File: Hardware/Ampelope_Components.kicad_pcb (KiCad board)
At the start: 4 copper layers, 60.5 x 81.6 mm, 117 parts, among them J1 Conn_01x12_Male, J2 Conn_01x12_Male, J3 Conn_01x12_Male, J4 Conn_01x12_Male, J5 Eurorack_16_pin_power, J6 Conn_01x02_Male, J7 SWD_Header, J8 USB_B_Micro, J9 Conn_01x02_Male, Q1 MMBT3906, Q2 MMBT3906, Q3 MMBT3906, Q4 MMBT3906, Q5 MMBT3906, U1 STM32G431RB, U2 AS3364, U3 LM1117-3.3, U4 TL074, U5 TL074, U6 TL074, Y1 8MHz 20pF

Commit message: Various schematic and PCB tidying
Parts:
- added R57: 1k, Resistor_SMD:R_0603_1608Metric_Pad0.98x0.95mm_HandSolder, F.Cu at (135.2, 72.4)
- added R58: 1k, Resistor_SMD:R_0603_1608Metric_Pad0.98x0.95mm_HandSolder, F.Cu at (135.2, 84.7)
- added R59: 1k, Resistor_SMD:R_0603_1608Metric_Pad0.98x0.95mm_HandSolder, F.Cu at (148.0, 83.0)
- added R60: 1k, Resistor_SMD:R_0603_1608Metric_Pad0.98x0.95mm_HandSolder, F.Cu at (148.0, 72.4)
- Y1: footprint Crystal:Crystal_SMD_5032-2Pin_5.0x3.2mm_HandSoldering -> Crystal:Crystal_SMD_0603-2Pin_6.0x3.5mm
- moved R51 3.64 mm to (148.0, 84.7), turned to 0 degrees
- moved R50 3.42 mm to (135.2, 83.0)
- moved R47 3.40 mm to (135.2, 70.7)
- moved R52 3.40 mm to (148.0, 70.7), turned to 0 degrees
- moved J9 2.75 mm to (152.7, 67.2), turned to -90 degrees
- moved R42 2.28 mm to (148.0, 75.8), turned to 0 degrees
- moved R36 2.28 mm to (135.2, 75.8), turned to 180 degrees
- moved R40 1.27 mm to (148.0, 79.6), turned to 0 degrees
- moved R38 1.27 mm to (135.2, 79.6), turned to 180 degrees
- moved R44 1.20 mm to (135.2, 81.3), turned to 180 degrees
- moved R45 1.20 mm to (148.0, 81.3), turned to 0 degrees
- moved TP5 1.20 mm to (140.4, 127.1)
- moved R43 0.98 mm to (135.2, 74.1), turned to 180 degrees
- moved R46 0.98 mm to (148.0, 74.1), turned to 0 degrees
- moved C6 0.05 mm to (147.6, 91.7)
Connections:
- R43 pad 1: /Env1_Out -> Net-(R43-Pad1)
- R44 pad 1: /Env2_Out -> Net-(R44-Pad1)
- R45 pad 1: /Env3_Out -> Net-(R45-Pad1)
- R46 pad 1: /Env4_Out -> Net-(R46-Pad1)
- R47 pad 1: /Env1_Out -> Net-(R43-Pad1)
- R50 pad 1: /Env2_Out -> Net-(R44-Pad1)
- R51 pad 1: /Env3_Out -> Net-(R45-Pad1)
- R52 pad 1: /Env4_Out -> Net-(R46-Pad1)
- U6 pad 1: /Env1_Out -> Net-(R43-Pad1)
- U6 pad 14: /Env4_Out -> Net-(R46-Pad1)
- U6 pad 7: /Env2_Out -> Net-(R44-Pad1)
- U6 pad 8: /Env3_Out -> Net-(R45-Pad1)
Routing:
- net VCC: track 130.0 -> 113.8 mm
- net /Env3_Out: track 30.4 -> 19.7 mm
- net /Env4_Out: track 14.0 -> 5.66 mm
- net Net-(R43-Pad1): track 0.00 -> 8.16 mm
- net Net-(R44-Pad1): track 0.00 -> 7.28 mm
- net Net-(R46-Pad1): track 0.00 -> 6.75 mm
- net Net-(R45-Pad1): track 0.00 -> 6.57 mm
- net /Led3_Out: track 24.2 -> 18.8 mm
- net /Led1_Out: track 26.4 -> 29.8 mm
- net /Led4_Out: track 17.3 -> 14.5 mm
- net +3V3: track 52.0 -> 49.3 mm, vias 20 -> 26
- net /Led2_Out: track 33.6 -> 36.2 mm
- net /Env1_Out: track 29.7 -> 27.6 mm
- net /Env2_DAC: track 31.5 -> 33.3 mm
- net GND: track 62.1 -> 63.5 mm, vias 36 -> 68
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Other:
- board text added: "A1i"
- board text added: "A1o"
- board text added: "A2i"
- board text added: "A2o"
- board text added: "A3i"
- board text added: "A3o"
- board text added: "A4i"
- board text added: "A4o"
- board text added: "Ampelope Components v1.0 Mountjoy Modular 2021"
- board text added: "Clk"
- board text added: "E1"
- board text added: "E1S"
- board text added: "E1T"
- board text added: "E2S"
- board text added: "E2T"
- board text added: "E3"
- board text added: "E3T"
- board text added: "E4S"
- board text added: "E4T"
- board text added: "E4s"
- board text added: "EaA"
- board text added: "EaD"
- board text added: "EaR"
- board text added: "EaS"
- board text added: "EbA"
- board text added: "EbD"
- board text added: "EbR"
- board text added: "EbS"
- board text added: "G1"
- board text added: "G2"
- board text added: "G3"
- board text added: "G4"
- board text added: "L1"
- board text added: "L2"
- board text added: "L3"
- board text added: "L4"
- board text added: "LFO"
- board text added: "Reset"

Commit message: Minor PCB cleanup
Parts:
- moved J9 5.46 mm to (147.2, 67.5), turned to 90 degrees
- moved R60 1.70 mm to (148.1, 70.7)
- moved R52 1.70 mm to (148.0, 72.4)
- moved R38 1.30 mm to (135.2, 78.3)
- moved R40 1.30 mm to (148.0, 78.3)
- moved R44 1.30 mm to (135.2, 80.0)
- moved R45 1.30 mm to (148.0, 80.0)
- moved R50 1.30 mm to (135.2, 81.7)
- moved R51 1.30 mm to (148.0, 83.4)
- moved R58 1.30 mm to (135.2, 83.4)
- moved R59 1.30 mm to (148.0, 81.7)
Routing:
- net /Env2_Out: track 33.0 -> 22.3 mm
- net /Env4_Out: track 5.66 -> 3.51 mm
- net /Led4_Out: track 14.5 -> 12.7 mm
- net /Led3_Out: track 18.8 -> 17.5 mm
- net /Env3_Out: track 19.7 -> 18.4 mm
- net /Env2_DAC: track 33.3 -> 34.6 mm
- net /Audio4_Out: track 38.2 -> 37.5 mm
- net Net-(R38-Pad1): track 5.38 -> 5.97 mm
- net Net-(R40-Pad1): track 5.38 -> 5.97 mm

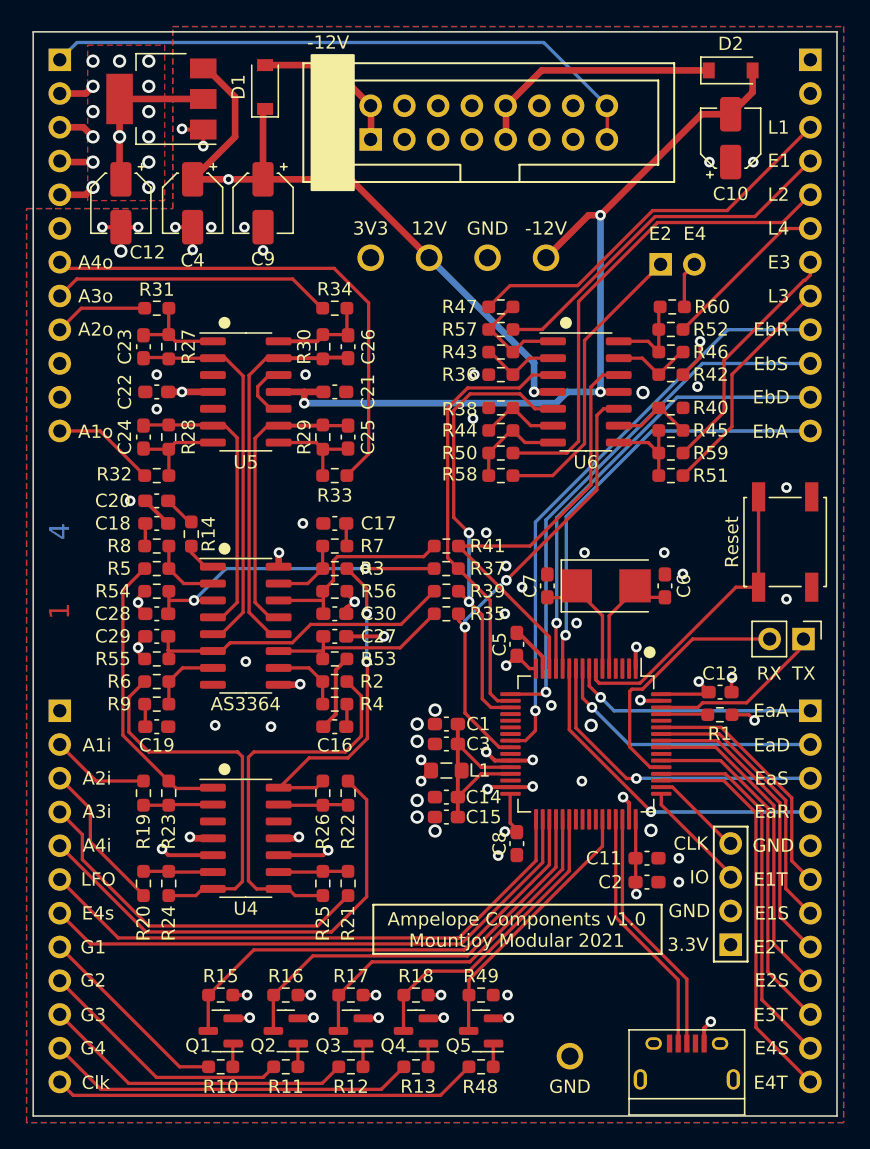
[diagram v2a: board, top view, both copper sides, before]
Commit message: Further PCB tidy up and DAC testing
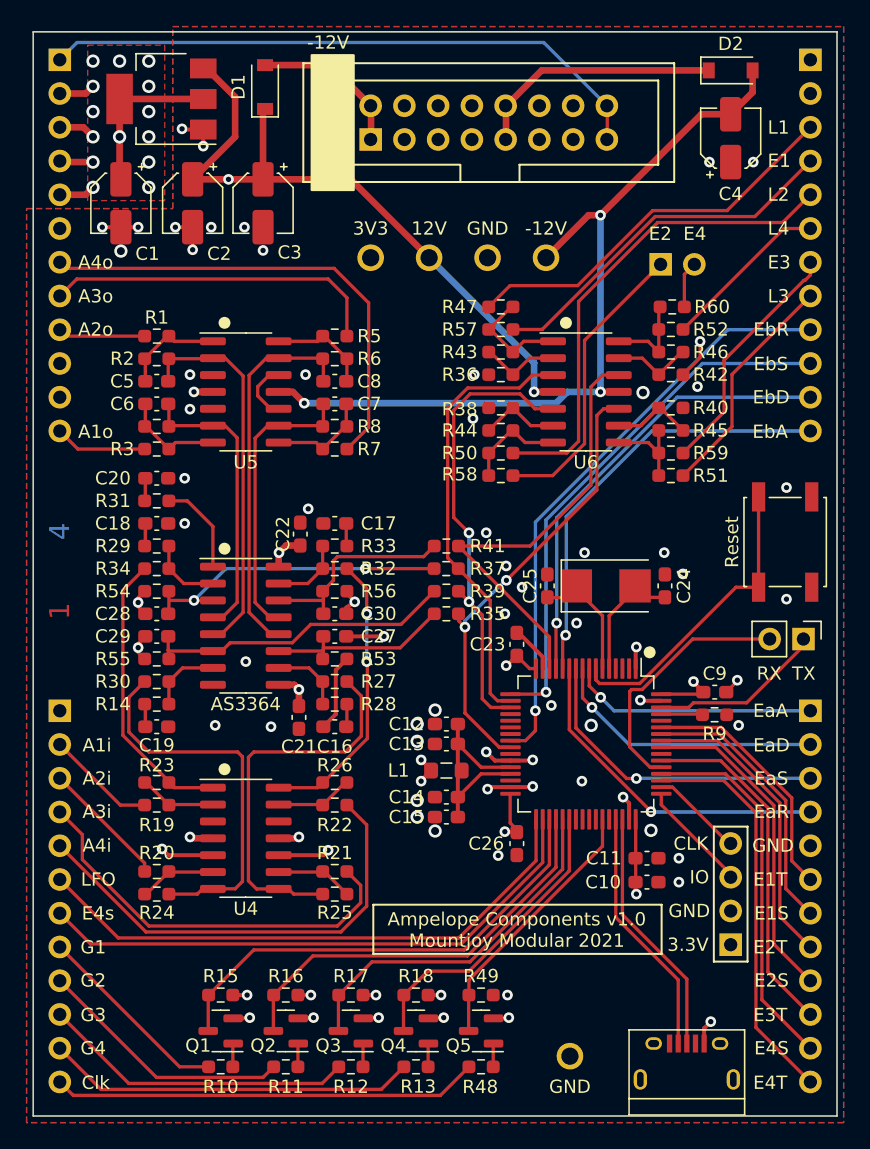
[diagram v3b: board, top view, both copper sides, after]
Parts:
- moved C21 24.6 mm to (120.0, 101.6), turned to -90 degrees
- moved C22 15.2 mm to (120.1, 87.8), turned to -90 degrees
- moved R31 3.61 mm to (109.3, 85.3), turned to 0 degrees
- moved C5 2.79 mm to (109.3, 76.3), turned to 180 degrees
- moved C8 2.79 mm to (122.7, 76.3), turned to 0 degrees
- moved C6 2.69 mm to (109.3, 78.0), turned to 180 degrees
- moved C7 2.69 mm to (122.7, 78.0), turned to 0 degrees
- moved R1 2.10 mm to (109.3, 72.9)
- moved R5 2.10 mm to (122.7, 72.9), turned to 180 degrees
- moved R3 2.00 mm to (109.3, 81.4)
- moved R7 2.00 mm to (122.7, 81.4)
- moved C20 1.70 mm to (109.3, 83.6), turned to 0 degrees
- moved R19 1.35 mm to (109.3, 108.2), turned to 180 degrees
- moved R22 1.35 mm to (122.7, 108.2), turned to 0 degrees
- moved R20 1.35 mm to (109.3, 113.2), turned to 180 degrees
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- renumbered C12 to C1, C2 to C10, C1 to C12, C3 to C13, C4 to C2, C5 to C23, C6 to C24, C7 to C25, C8 to C26, C9 to C3, C10 to C4, C23 to C5, C24 to C6, C25 to C7, C26 to C8, C13 to C9, R31 to R1, R9 to R14, R27 to R2, R2 to R27, R4 to R28, R8 to R29, R32 to R3, R6 to R30, R14 to R31, R3 to R32, R7 to R33, R5 to R34, R28 to R4, R34 to R5, R30 to R6, R33 to R7, R29 to R8, R1 to R9
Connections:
- C22 pad 1: VCC -> GND
- C22 pad 2: GND -> VCC
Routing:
- net Net-(R31-Pad2): track 1.84 -> 7.14 mm
- net /Audio3_Out: track 21.2 -> 25.6 mm
- net GND: track 63.5 -> 59.3 mm, vias 68 -> 69
- net /Audio4_In_Buff: track 25.2 -> 21.6 mm
- net /Audio3_In: track 27.3 -> 30.8 mm
- net /Audio4_Out: track 37.5 -> 35.5 mm
- net /Audio2_In: track 11.4 -> 9.67 mm
- net /Audio4_In: track 36.2 -> 34.8 mm
- net /Audio2_Out: track 7.06 -> 5.91 mm
- net /Audio1_VCA: track 21.4 -> 20.4 mm
- net VEE: track 101.4 -> 100.4 mm
- net /Audio1_In: track 7.44 -> 8.28 mm
- net Net-(R19-Pad1): track 4.85 -> 5.68 mm
- net /Audio1_Out: track 7.78 -> 6.95 mm
- net Net-(R22-Pad1): track 4.98 -> 5.68 mm
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
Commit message: Changed input protection diodes back to 3904s; prepared gerbers
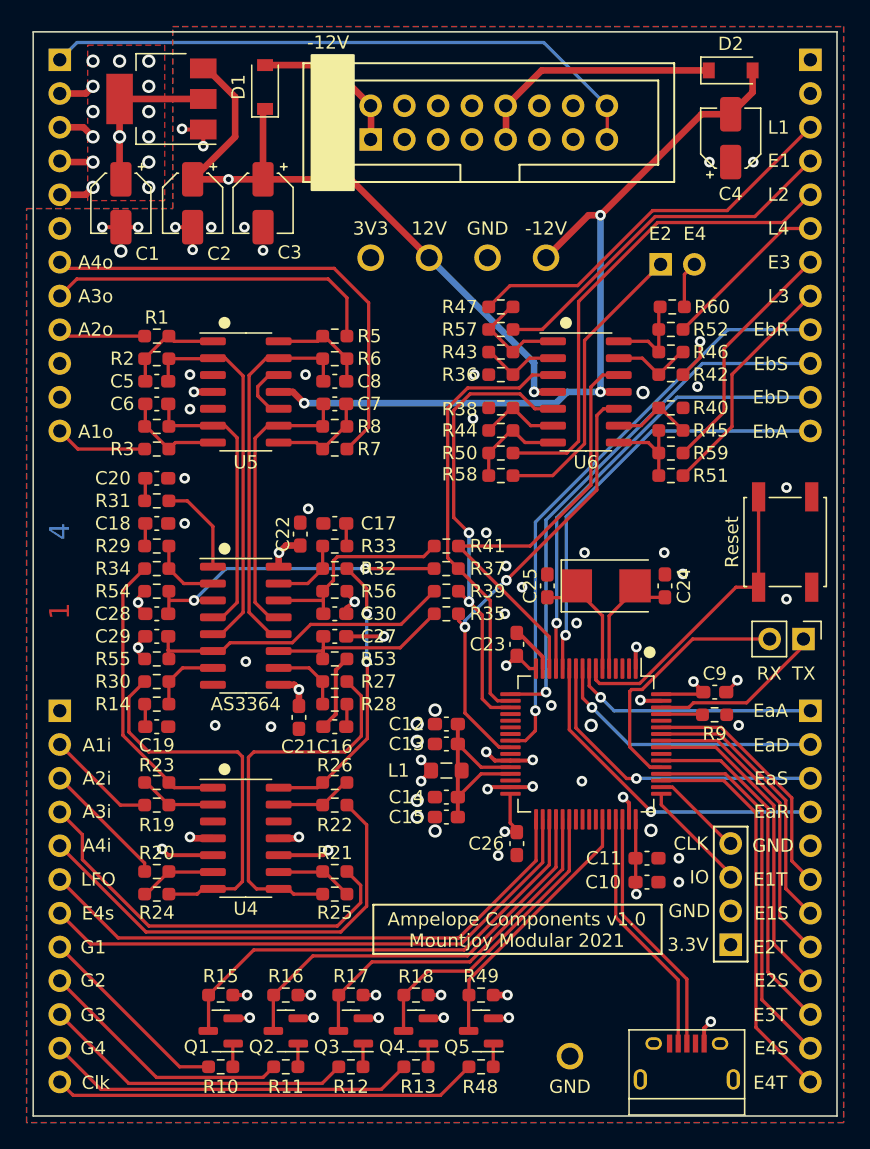
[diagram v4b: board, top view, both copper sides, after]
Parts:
- Q1, Q2, Q3, Q4, Q5: value MMBT3906 -> MMBT3904
- R10, R11, R12, R13, R15, R16, R17, R18, R48, R49: value 1k -> 4k7
- turned R18 to 180 degrees
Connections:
- Q1 pad 2: +3V3 -> GND
- Q2 pad 2: +3V3 -> GND
- Q3 pad 2: +3V3 -> GND
- Q4 pad 2: +3V3 -> GND
- Q5 pad 2: +3V3 -> GND
- R15 pad 2: GND -> +3V3
- R16 pad 2: GND -> +3V3
- R17 pad 2: GND -> +3V3
- R18 pad 1: /Gate4_Inv -> +3V3
- R18 pad 2: GND -> /Gate4_Inv
- R49 pad 2: GND -> +3V3
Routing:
- net GND: track 59.3 -> 61.2 mm
- net +3V3: track 49.1 -> 48.2 mm

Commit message: Prepared gerbers for pcb manufacture
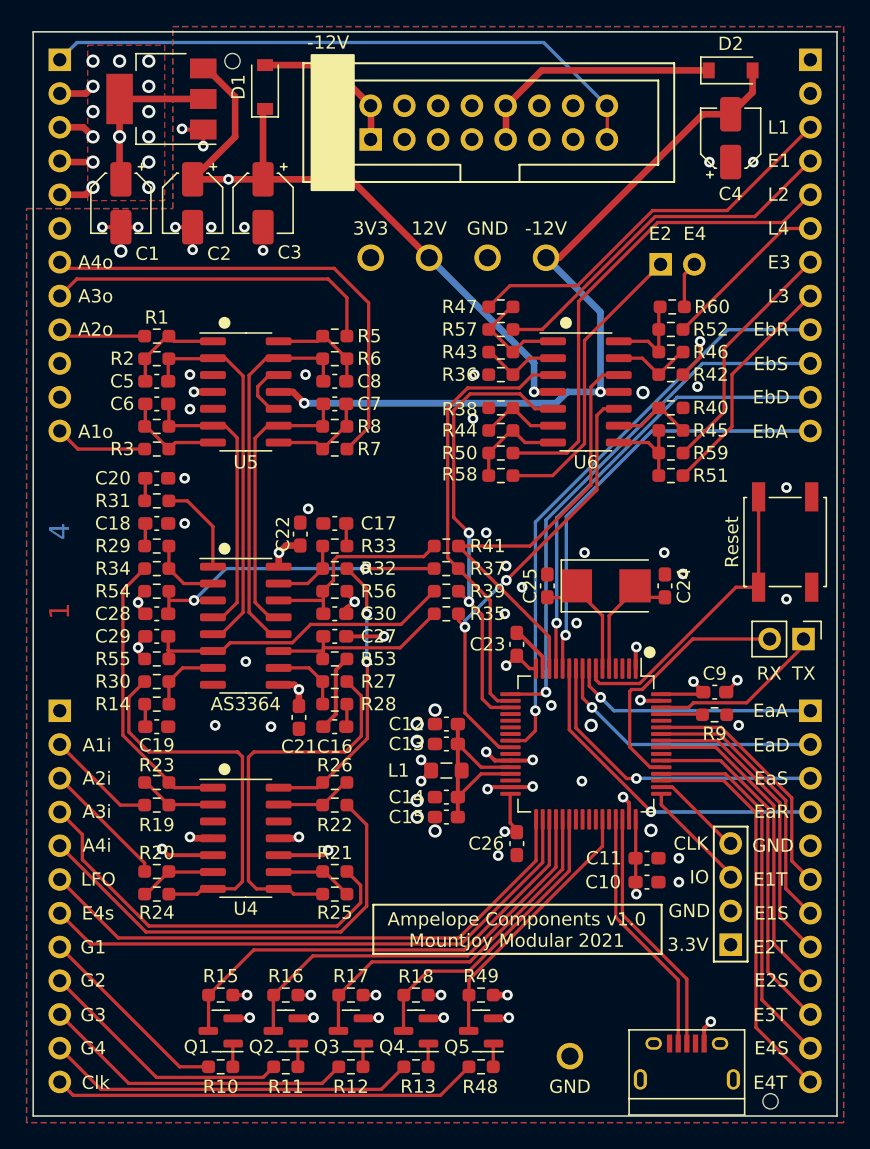
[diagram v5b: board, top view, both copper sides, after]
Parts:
- added FID2: JLC_Tooling_Hole, Custom_Footprints:JLC_SMT_Tooling_Hole, F.Cu at (155.5, 130.5)
- added FID3: JLC_Tooling_Hole, Custom_Footprints:JLC_SMT_Tooling_Hole, F.Cu at (115.0, 52.2)
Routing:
- net VEE: track 100.4 -> 98.9 mm, vias 5 -> 4
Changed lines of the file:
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@@
     )
   )
+  (footprint "Custom_Footprints:JLC_SMT_Tooling_Hole" (layer "F.Cu")
+    (at 115 52.2)
+    (descr "Mounting Hole 2.2mm, no annular, M2")
+    (tags "mounting hole 2.2mm no annular m2")
+    (property "Sheetfile" "Ampelope_Components.kicad_sch")
+    (property "Sheetname" "")
+    (attr exclude_from_pos_files)
+    (fp_text reference "FID3" (at 0 -3.2) (layer "F.SilkS") hide
+      (effects (font (size 1 1) (thickness 0.15)))
+    )
+    (fp_text value "JLC_Tooling_Hole" (at 0 3.2) (layer "F.Fab") hide
+      (effects (font (size 1 1) (thickness 0.15)))
+    )
+    (fp_text user "${REFERENCE}" (at 0 -3.2) (layer "F.Fab") hide
+      (effects (font (size 1 1) (thickness 0.15)))
+    )
+    (fp_circle (center 0 0) (end 0.825 0) (layer "Dwgs.User") (width 0.1) (fill none))
+    (fp_circle (center 0 0) (end 0.825 0) (layer "F.CrtYd") (width 0.05) (fill none))
+    (pad "" np_thru_hole circle (at 0 0) (size 1.152 1.152) (drill 1.152) (layers F&B.Cu *.Mask)
+      (clearance 0.25))
+  )
   (footprint "Capacitor_SMD:C_0603_1608Metric_Pad1.08x0.95mm_HandSolder" (layer "F.Cu")
     (at 109.3 87)
@@
     (descr "SOT, 3 Pin (https://www.jedec.org/system/files/docs/to-236h.pdf variant AB), generated with kicad-footprint-generator ipc_gullwing_generator.py")
     (tags "SOT TO_SOT_SMD")
+    (property "Part_Number" "C20526")
     (property "Sheetfile" "Ampelope_Components.kicad_sch")
     (property "Sheetname" "")
@@
     (descr "SOT, 3 Pin (https://www.jedec.org/system/files/docs/to-236h.pdf variant AB), generated with kicad-footprint-generator ipc_gullwing_generator.py")
     (tags "SOT TO_SOT_SMD")
+    (property "Part_Number" "C20526")
     (property "Sheetfile" "Ampelope_Components.kicad_sch")
     (property "Sheetname" "")
@@
     (descr "SOT, 3 Pin (https://www.jedec.org/system/files/docs/to-236h.pdf variant AB), generated with kicad-footprint-generator ipc_gullwing_generator.py")
     (tags "SOT TO_SOT_SMD")
+    (property "Part_Number" "C20526")
     (property "Sheetfile" "Ampelope_Components.kicad_sch")
     (property "Sheetname" "")
@@
     (descr "SOT, 3 Pin (https://www.jedec.org/system/files/docs/to-236h.pdf variant AB), generated with kicad-footprint-generator ipc_gullwing_generator.py")
     (tags "SOT TO_SOT_SMD")
+    (property "Part_Number" "C20526")
     (property "Sheetfile" "Ampelope_Components.kicad_sch")
     (property "Sheetname" "")
@@
     )
   )
+  (footprint "Custom_Footprints:JLC_SMT_Tooling_Hole" (layer "F.Cu")
+    (at 155.5 130.5)
+    (descr "Mounting Hole 2.2mm, no annular, M2")
+    (tags "mounting hole 2.2mm no annular m2")
+    (property "Sheetfile" "Ampelope_Components.kicad_sch")
+    (property "Sheetname" "")
+    (attr exclude_from_pos_files)
+    (fp_text reference "FID2" (at 0 -3.2) (layer "F.SilkS") hide
+      (effects (font (size 1 1) (thickness 0.15)))
+    )
+    (fp_text value "JLC_Tooling_Hole" (at 0 3.2) (layer "F.Fab") hide
+      (effects (font (size 1 1) (thickness 0.15)))
+    )
+    (fp_text user "${REFERENCE}" (at 0 -3.2) (layer "F.Fab") hide
+      (effects (font (size 1 1) (thickness 0.15)))
+    )
+    (fp_circle (center 0 0) (end 0.825 0) (layer "Dwgs.User") (width 0.1) (fill none))
+    (fp_circle (center 0 0) (end 0.825 0) (layer "F.CrtYd") (width 0.05) (fill none))
+    (pad "" np_thru_hole circle (at 0 0) (size 1.152 1.152) (drill 1.152) (layers F&B.Cu *.Mask)
+      (clearance 0.25))
+  )
   (footprint "Resistor_SMD:R_0603_1608Metric_Pad0.98x0.95mm_HandSolder" (layer "F.Cu")
     (at 123.9125 122.5)
@@
     (descr "SOT, 3 Pin (https://www.jedec.org/system/files/docs/to-236h.pdf variant AB), generated with kicad-footprint-generator ipc_gullwing_generator.py")
     (tags "SOT TO_SOT_SMD")
+    (property "Part_Number" "C20526")
     (property "Sheetfile" "Ampelope_Components.kicad_sch")
     (property "Sheetname" "")
@@
   (segment (start 118.475 99.145) (end 119.645 99.145) (width 0.5) (layer "F.Cu") (net 3))
   (segment (start 154.15 52.9) (end 154.15 54.55) (width 0.5) (layer "F.Cu") (net 3))
-  (segment (start 150.3 56.2) (end 152.5 56.2) (width 0.5) (layer "F.Cu") (net 3))
-  (segment (start 142.7 63.8) (end 150.3 56.2) (width 0.5) (layer "F.Cu") (net 3))
+  (segment (start 150.4 56.2) (end 152.5 56.2) (width 0.5) (layer "F.Cu") (net 3))
   (segment (start 120 110.6) (end 119.9 110.7) (width 0.5) (layer "F.Cu") (net 3))
   (segment (start 119.645 99.145) (end 120 99.5) (width 0.5) (layer "F.Cu") (net 3))
   (segment (start 154.15 54.55) (end 152.5 56.2) (width 0.5) (layer "F.Cu") (net 3))
+  (segment (start 138.6 67) (end 139.6 67) (width 0.5) (layer "F.Cu") (net 3))
   (segment (start 119.5505 77.1) (end 118.475 77.1) (width 0.5) (layer "F.Cu") (net 3))
   (segment (start 142.7 77.1) (end 144.075 77.1) (width 0.5) (layer "F.Cu") (net 3))
-  (segment (start 141.8 63.8) (end 142.7 63.8) (width 0.5) (layer "F.Cu") (net 3))
+  (segment (start 139.6 67) (end 150.4 56.2) (width 0.5) (layer "F.Cu") (net 3))
   (segment (start 119.9 110.7) (end 118.475 110.7) (width 0.5) (layer "F.Cu") (net 3))
-  (segment (start 138.6 67) (end 141.8 63.8) (width 0.5) (layer "F.Cu") (net 3))
   (via (at 142.7 77.1) (size 0.8) (drill 0.4) (layers "F.Cu" "B.Cu") (net 3))
   (via (at 120 110.6) (size 0.8) (drill 0.4) (layers "F.Cu" "B.Cu") (net 3))
   (via (at 120 99.5) (size 0.8) (drill 0.4) (layers "F.Cu" "B.Cu") (net 3))
   (via (at 120.4 77.9495) (size 0.8) (drill 0.4) (layers "F.Cu" "B.Cu") (net 3))
-  (via (at 142.7 63.8) (size 0.8) (drill 0.4) (layers "F.Cu" "B.Cu") (net 3))
   (segment (start 120.1 99.1) (end 122 97.2) (width 1) (layer "In2.Cu") (net 3))
   (segment (start 122 79.5495) (end 120.4 77.9495) (width 1) (layer "In2.Cu") (net 3))
   (segment (start 122 97.2) (end 122 79.5495) (width 1) (layer "In2.Cu") (net 3))
   (segment (start 120 110.6) (end 120 99.2) (width 1) (layer "In2.Cu") (net 3))
+  (segment (start 138.6 67) (end 142.7 71.1) (width 0.5) (layer "B.Cu") (net 3))
   (segment (start 142.7 77.1) (end 140.2 77.1) (width 0.5) (layer "B.Cu") (net 3))
   (segment (start 139.3505 77.9495) (end 120.4 77.9495) (width 0.5) (layer "B.Cu") (net 3))
   (segment (start 140.2 77.1) (end 139.3505 77.9495) (width 0.5) (layer "B.Cu") (net 3))
-  (segment (start 142.7 63.8) (end 142.7 77.1) (width 0.5) (layer "B.Cu") (net 3))
+  (segment (start 142.7 71.1) (end 142.7 77.1) (width 0.5) (layer "B.Cu") (net 3))
   (segment (start 104.5 57.9) (end 103.78 57.18) (width 0.5) (layer "F.Cu") (net 4))
   (segment (start 136.4 97) (end 135.6 97.7) (width 0.3) (layer "F.Cu") (net 4))
@@
   (segment (start 132.44904 119.10096) (end 138.85 112.7) (width 0.25) (layer "F.Cu") (net 29))
   (segment (start 113.2 122.5) (end 113.2 125.175) (width 0.25) (layer "F.Cu") (net 29))
-  (segment (start 113.2 125.175) (end 113.175 125.2) (width 0.25) (layer "F.Cu") (net 29))
   (segment (start 138.85 112.7) (end 138.85 109.275) (width 0.25) (layer "F.Cu") (net 29))
   (segment (start 113.525 96.605) (end 110.23 96.605) (width 0.25) (layer "F.Cu") (net 30))
